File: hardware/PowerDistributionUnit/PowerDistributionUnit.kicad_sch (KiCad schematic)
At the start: 0 parts

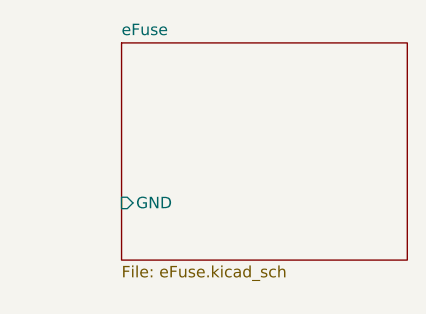
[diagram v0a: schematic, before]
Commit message: Added components on eFuse sheet
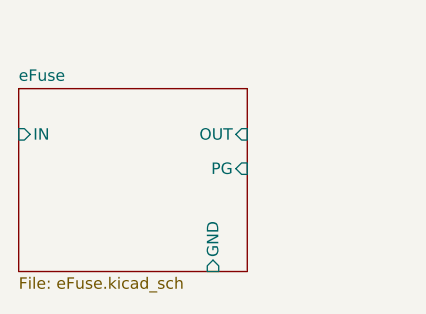
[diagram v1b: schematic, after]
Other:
- sheet eFuse ports: added IN, OUT, PG; removed none
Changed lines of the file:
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@@
 	(paper "A4")
 	(sheet
-		(at 40.64 20.32)
-		(size 31.75 24.13)
+		(at 29.21 25.4)
+		(size 25.4 20.32)
 		(fields_autoplaced yes)
 		(stroke
@@
 		)
 		(property "Sheetname" "eFuse"
-			(at 40.64 19.6084 0)
+			(at 29.21 24.6884 0)
 			(effects
 				(font
@@
 		)
 		(property "Sheetfile" "eFuse.kicad_sch"
-			(at 40.64 45.0346 0)
+			(at 29.21 46.3046 0)
 			(effects
 				(font
@@
 		)
 		(pin "GND" input
-			(at 40.64 38.1 180)
+			(at 50.8 45.72 270)
 			(effects
 				(font
@@
 			)
 		)
+		(pin "OUT" input
+			(at 54.61 30.48 0)
+			(effects
+				(font
+					(size 1.27 1.27)
+				)
+				(justify right)
+			)
+		)
+		(pin "IN" input
+			(at 29.21 30.48 180)
+			(effects
+				(font
+					(size 1.27 1.27)
+				)
+				(justify left)
+			)
+		)
+		(pin "PG" input
+			(at 54.61 34.29 0)
+			(effects
+				(font
+					(size 1.27 1.27)
+				)
+				(justify right)
+			)
+		)

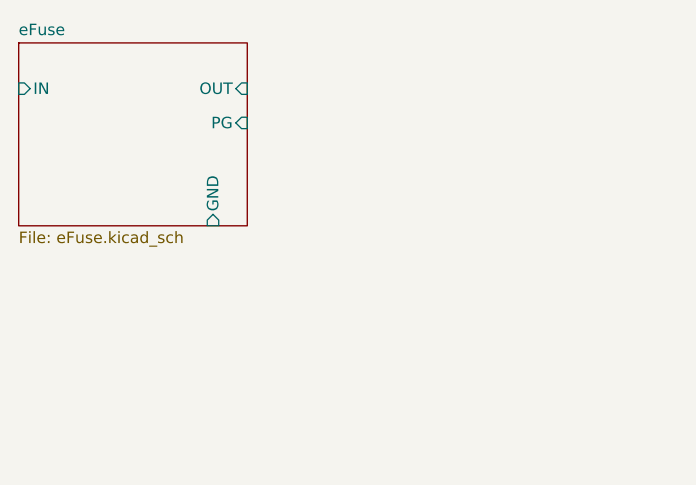
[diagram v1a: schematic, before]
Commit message: aesthetic updates (wire colors, slimmed digital pot symbol), added slight documentation on eFuse retries to schematic, prepared for digital pot wiring a bit, other fun stuff
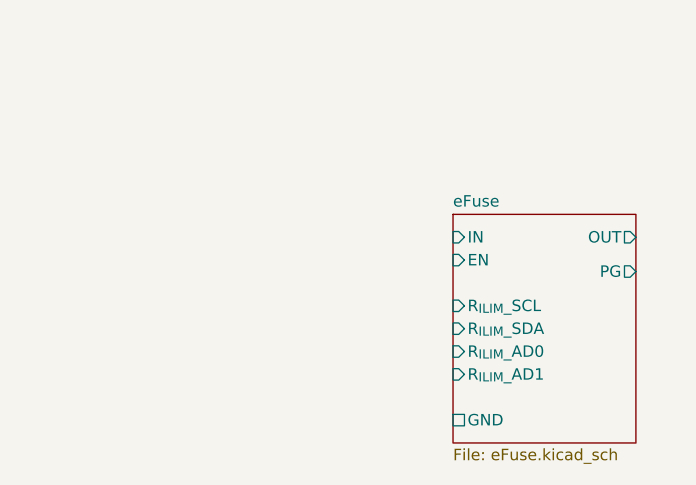
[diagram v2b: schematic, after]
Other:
- sheet eFuse ports: added EN, R_{ILIM}_AD0, R_{ILIM}_AD1, R_{ILIM}_SCL, R_{ILIM}_SDA; removed none
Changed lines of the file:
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@@
 	(paper "A4")
 	(sheet
-		(at 29.21 25.4)
-		(size 25.4 20.32)
+		(at 77.47 44.45)
+		(size 20.32 25.4)
 		(fields_autoplaced yes)
 		(stroke
 			(width 0.1524)
 			(type solid)
+			(color 0 0 0 1)
 		)
 		(fill
-			(color 0 0 0 0.0000)
+			(color 223 223 223 1.0000)
 		)
 		(property "Sheetname" "eFuse"
-			(at 29.21 24.6884 0)
+			(at 77.47 43.7384 0)
 			(effects
 				(font
@@
 		)
 		(property "Sheetfile" "eFuse.kicad_sch"
-			(at 29.21 46.3046 0)
+			(at 77.47 70.4346 0)
 			(effects
 				(font
@@
 			)
 		)
-		(pin "GND" input
-			(at 50.8 45.72 270)
+		(pin "GND" passive
+			(at 77.47 67.31 180)
 			(effects
 				(font
@@
 			)
 		)
-		(pin "OUT" input
-			(at 54.61 30.48 0)
+		(pin "OUT" output
+			(at 97.79 46.99 0)
 			(effects
 				(font
@@
 		)
 		(pin "IN" input
-			(at 29.21 30.48 180)
+			(at 77.47 46.99 180)
 			(effects
 				(font
@@
 			)
 		)
-		(pin "PG" input
-			(at 54.61 34.29 0)
+		(pin "PG" output
+			(at 97.79 50.8 0)
 			(effects
 				(font
@@
 			)
 		)
+		(pin "EN" input
+			(at 77.47 49.53 180)
+			(effects
+				(font
+					(size 1.27 1.27)
+				)
+				(justify left)
+			)
+		)
+		(pin "R_{ILIM}_SCL" input
+			(at 77.47 54.61 180)
+			(effects
+				(font
+					(size 1.27 1.27)
+				)
+				(justify left)
+			)
+		)
+		(pin "R_{ILIM}_SDA" input
+			(at 77.47 57.15 180)
+			(effects
+				(font
+					(size 1.27 1.27)
+				)
+				(justify left)
+			)
+		)
+		(pin "R_{ILIM}_AD1" input
+			(at 77.47 62.23 180)
+			(effects
+				(font
+					(size 1.27 1.27)
+				)
+				(justify left)
+			)
+		)
+		(pin "R_{ILIM}_AD0" input
+			(at 77.47 59.69 180)
+			(effects
+				(font
+					(size 1.27 1.27)
+				)
+				(justify left)
+			)
+		)

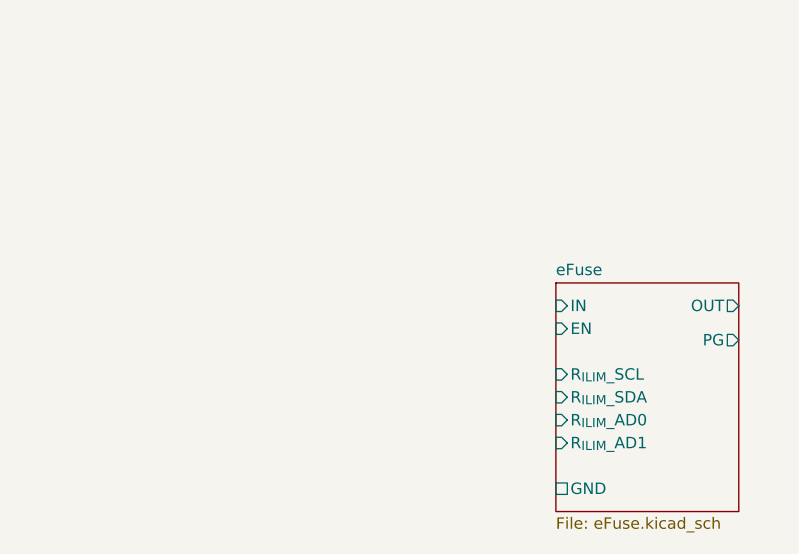
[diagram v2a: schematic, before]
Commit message: Finished eFuse schematic and now connecting everything
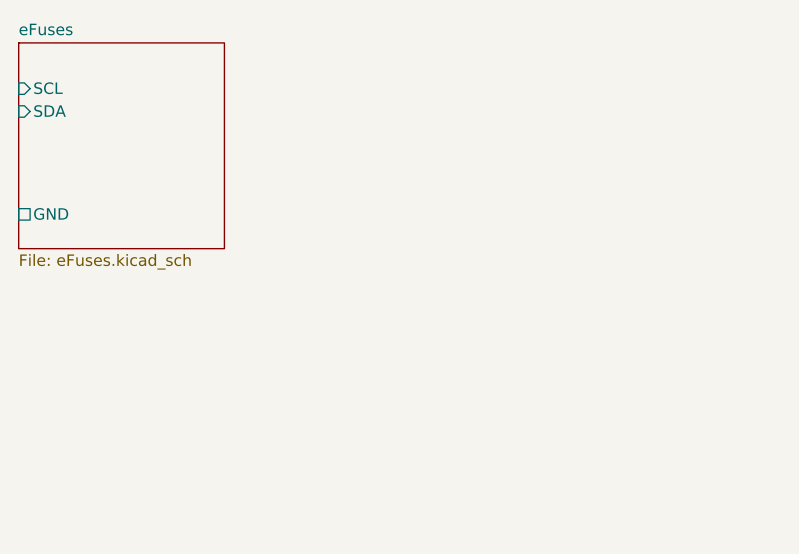
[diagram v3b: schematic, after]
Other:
- removed sheet eFuse
- added sheet eFuses (eFuses.kicad_sch)
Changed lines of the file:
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@@
 	(paper "A4")
 	(sheet
-		(at 77.47 44.45)
-		(size 20.32 25.4)
+		(at 17.78 17.78)
+		(size 22.86 22.86)
 		(fields_autoplaced yes)
 		(stroke
 			(width 0.1524)
 			(type solid)
-			(color 0 0 0 1)
 		)
 		(fill
-			(color 223 223 223 1.0000)
+			(color 255 229 191 1.0000)
 		)
-		(property "Sheetname" "eFuse"
-			(at 77.47 43.7384 0)
+		(property "Sheetname" "eFuses"
+			(at 17.78 17.0684 0)
 			(effects
 				(font
@@
 			)
 		)
-		(property "Sheetfile" "eFuse.kicad_sch"
-			(at 77.47 70.4346 0)
+		(property "Sheetfile" "eFuses.kicad_sch"
+			(at 17.78 41.2246 0)
 			(effects
 				(font
@@
 		)
 		(pin "GND" passive
-			(at 77.47 67.31 180)
+			(at 17.78 36.83 180)
 			(effects
 				(font
@@
 			)
 		)
-		(pin "OUT" output
-			(at 97.79 46.99 0)
-			(effects
-				(font
-					(size 1.27 1.27)
-				)
-				(justify right)
-			)
-		)
-		(pin "IN" input
-			(at 77.47 46.99 180)
+		(pin "SCL" input
+			(at 17.78 22.86 180)
 			(effects
 				(font
@@
 			)
 		)
-		(pin "PG" output
-			(at 97.79 50.8 0)
-			(effects
-				(font
-					(size 1.27 1.27)
-				)
-				(justify right)
-			)
-		)
-		(pin "EN" input
-			(at 77.47 49.53 180)
-			(effects
-				(font
-					(size 1.27 1.27)
-				)
-				(justify left)
-			)
-		)
-		(pin "R_{ILIM}_SCL" input
-			(at 77.47 54.61 180)
-			(effects
-				(font
-					(size 1.27 1.27)
-				)
-				(justify left)
-			)
-		)
-		(pin "R_{ILIM}_SDA" input
-			(at 77.47 57.15 180)
-			(effects
-				(font
-					(size 1.27 1.27)
-				)
-				(justify left)
-			)
-		)
-		(pin "R_{ILIM}_AD1" input
-			(at 77.47 62.23 180)
-			(effects
-				(font
-					(size 1.27 1.27)
-				)
-				(justify left)
-			)
-		)
-		(pin "R_{ILIM}_AD0" input
-			(at 77.47 59.69 180)
+		(pin "SDA" input
+			(at 17.78 25.4 180)
 			(effects
 				(font
@@
 			(project "PowerDistributionUnit"
 				(path "/93fa4ef0-f02c-4535-aca9-c62461ff58dd"
-					(page "2")
+					(page "8")
 				)
 			)

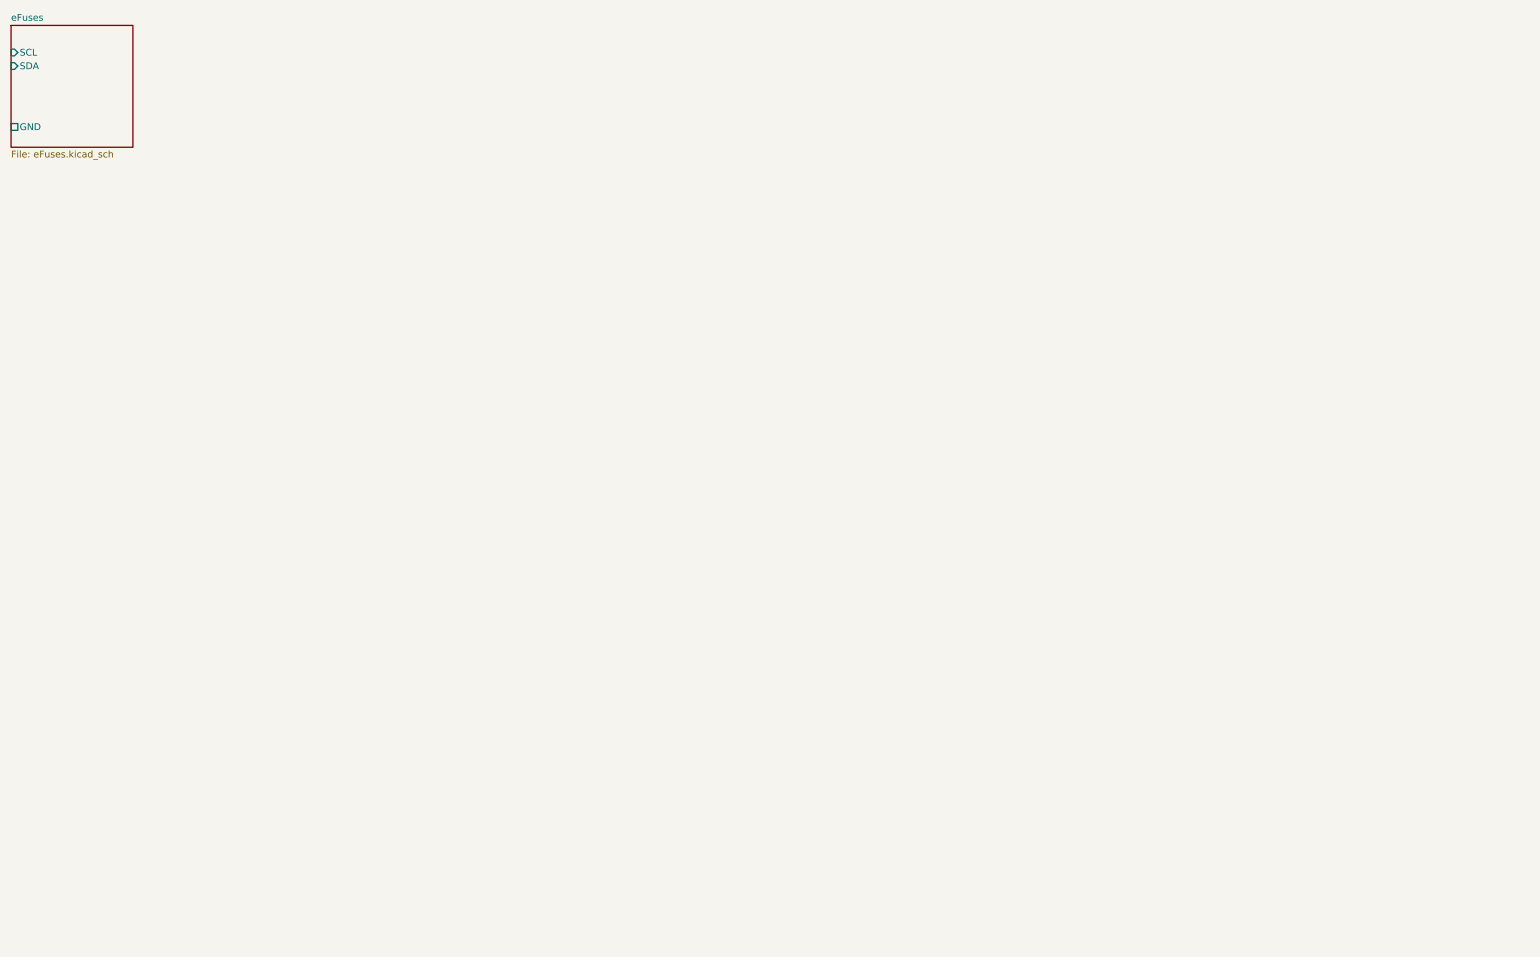
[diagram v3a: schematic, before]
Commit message: split off monitoring to its own sheet, continued connecting hardware and adding symbols
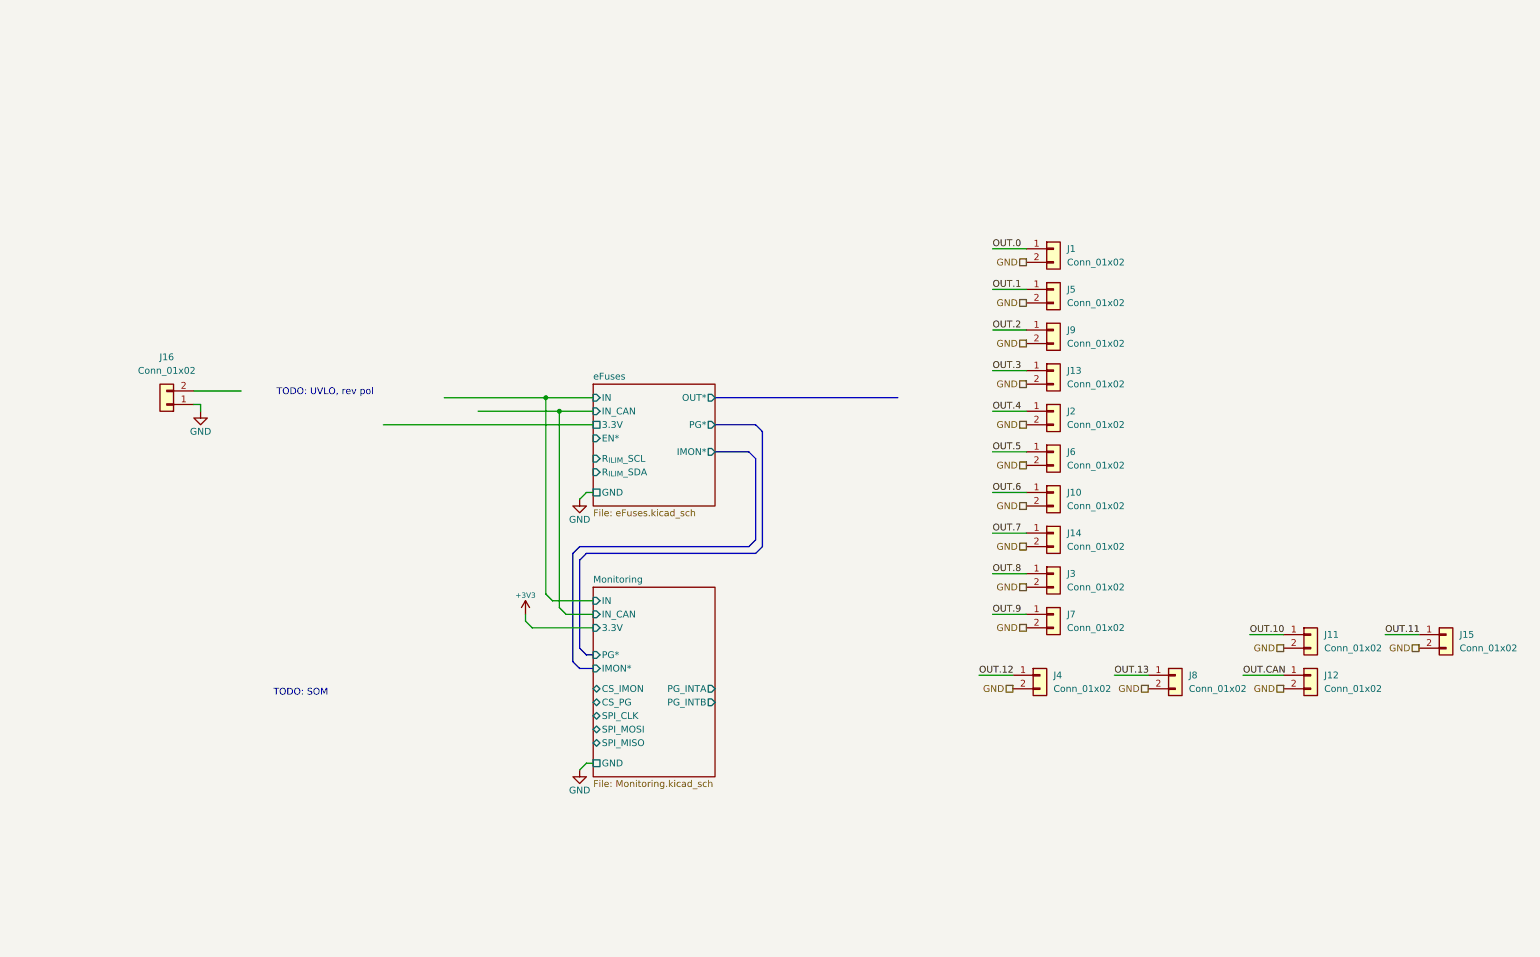
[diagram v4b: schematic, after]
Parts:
- added J1, J10, J11, J12, J13, J14, J15, J16, J2, J3, J4, J5, J6, J7, J8, J9: Conn_01x02, symbol Connector_Generic:Conn_01x02
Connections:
- new net GND: J1.2 (Pin_2), J10.2 (Pin_2), J11.2 (Pin_2), J12.2 (Pin_2), J13.2 (Pin_2), J14.2 (Pin_2), J15.2 (Pin_2), J16.1 (Pin_1), J2.2 (Pin_2), J3.2 (Pin_2), J4.2 (Pin_2), J5.2 (Pin_2), J6.2 (Pin_2), J7.2 (Pin_2), J8.2 (Pin_2), J9.2 (Pin_2)
- new net OUT.0: J1.1 (Pin_1)
- new net OUT.1: J5.1 (Pin_1)
- new net OUT.10: J11.1 (Pin_1)
- new net OUT.11: J15.1 (Pin_1)
- new net OUT.12: J4.1 (Pin_1)
- new net OUT.13: J8.1 (Pin_1)
- new net OUT.2: J9.1 (Pin_1)
- new net OUT.3: J13.1 (Pin_1)
- new net OUT.4: J2.1 (Pin_1)
- new net OUT.5: J6.1 (Pin_1)
- new net OUT.6: J10.1 (Pin_1)
- new net OUT.7: J14.1 (Pin_1)
- new net OUT.8: J3.1 (Pin_1)
- new net OUT.9: J7.1 (Pin_1)
- new net OUT.CAN: J12.1 (Pin_1)
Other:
- added sheet Monitoring (Monitoring.kicad_sch)
- sheet eFuses ports: added 3.3V, EN*, IMON*, IN, IN_CAN, OUT*, PG*, R_{ILIM}_SCL, R_{ILIM}_SDA; removed SCL, SDA
- note added: "TODO: SOM"
- note added: "TODO: UVLO, rev pol"

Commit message: wired up output connectors
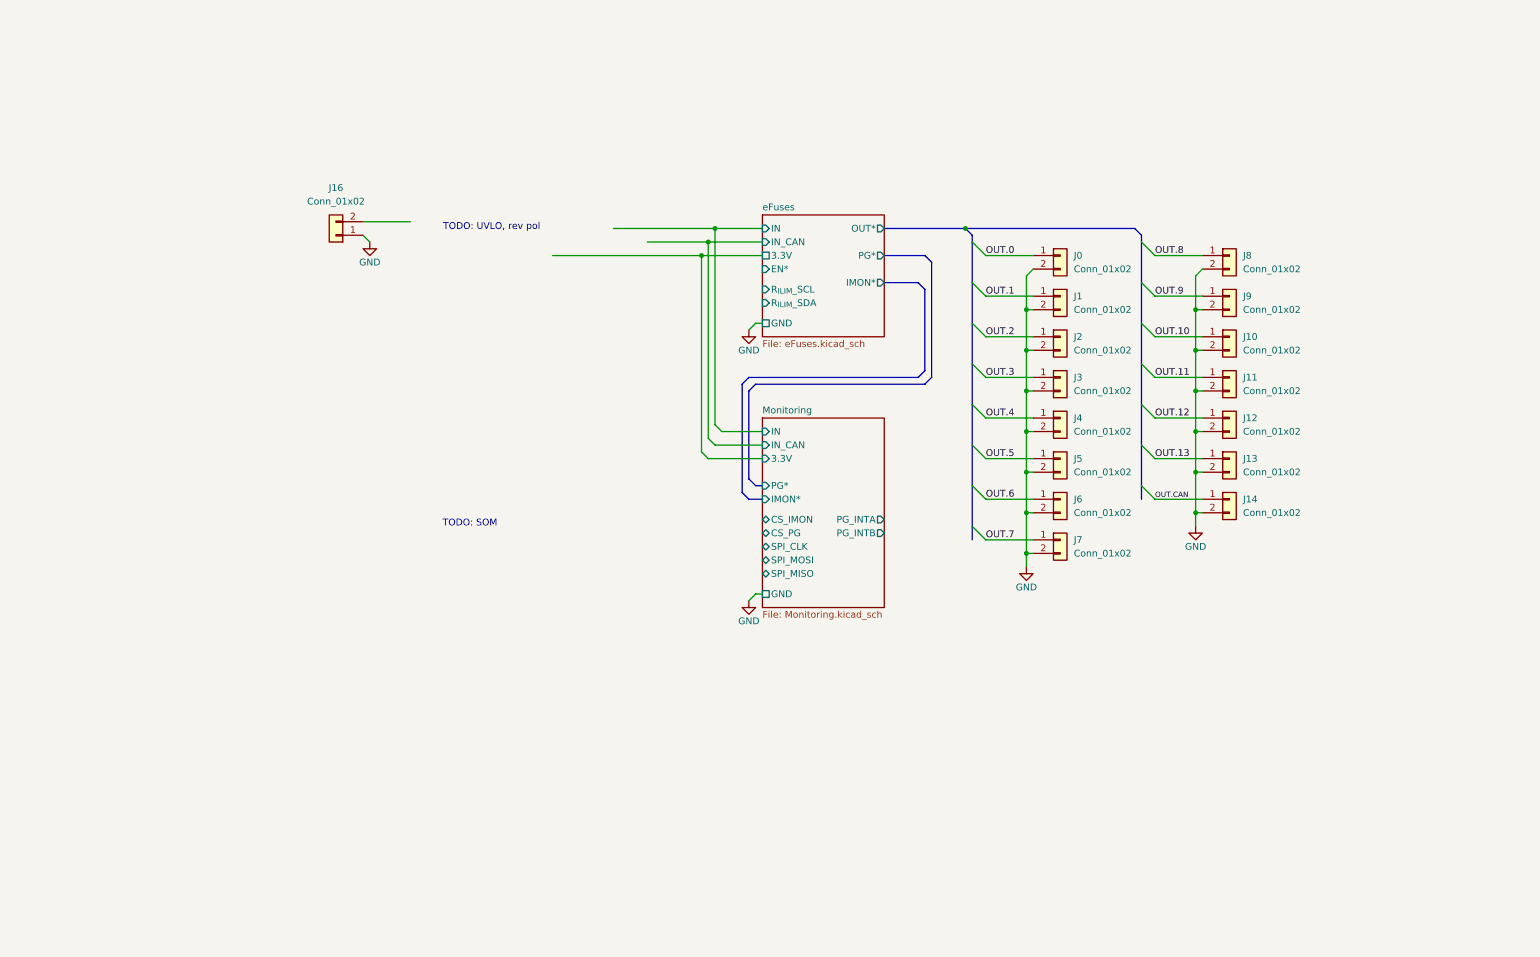
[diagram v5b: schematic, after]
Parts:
- renumbered J1 to J0, J5 to J1, J11 to J10, J15 to J11, J4 to J12, J8 to J13, J12 to J14, J9 to J2, J13 to J3, J2 to J4, J6 to J5, J10 to J6, J14 to J7, J3 to J8, J7 to J9
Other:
- moved on the sheet: J0, J1, J10, J11, J12, J13, J14, J16, J2, J3, J4, J5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
